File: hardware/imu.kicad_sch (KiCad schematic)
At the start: 4 parts, among them U9 LSM6DSV16XTR

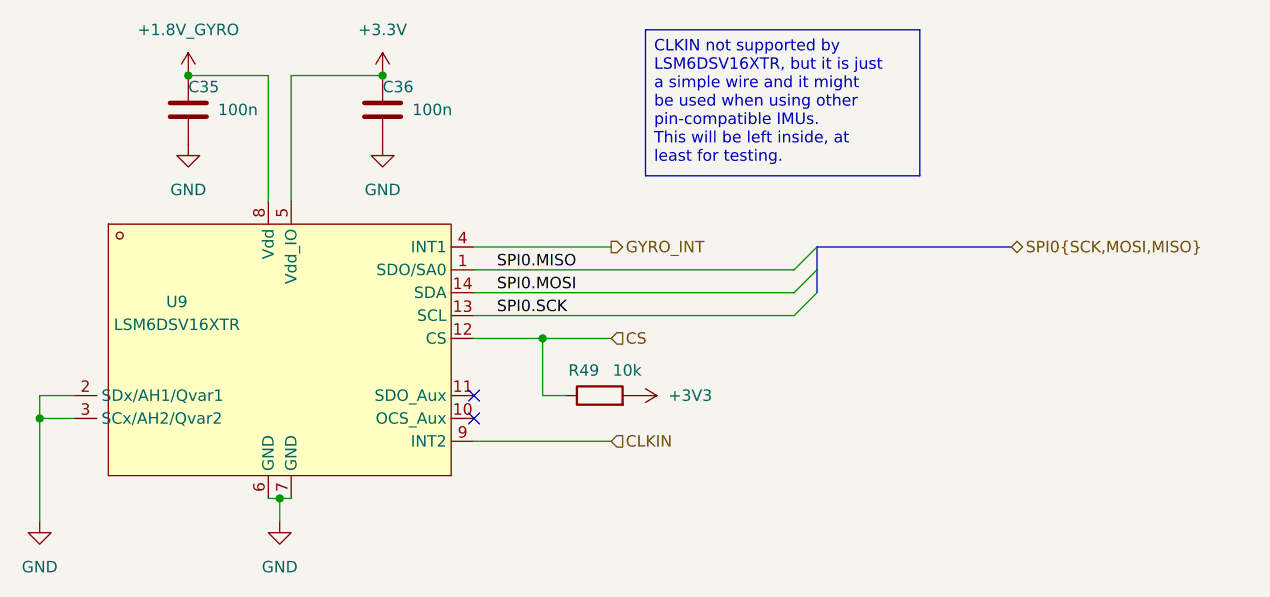
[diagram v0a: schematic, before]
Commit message: move changes from mini over to "maxi"
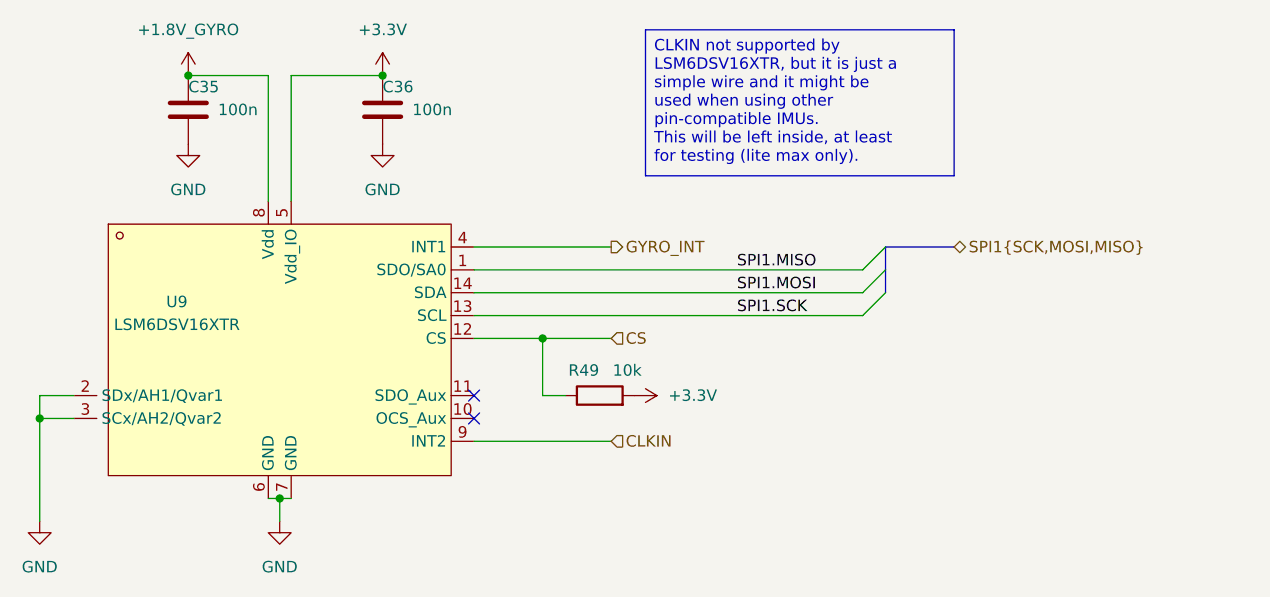
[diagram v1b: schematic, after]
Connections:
- net +3V3 is gone; now on net +3.3V: R49.2
- net SPI0.MISO renamed SPI1.MISO
- net SPI0.MOSI renamed SPI1.MOSI
- net SPI0.SCK renamed SPI1.SCK
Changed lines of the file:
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@@
 	(generator_version "10.0")
 	(paper "A5")
-	(text_box "CLKIN not supported by LSM6DSV16XTR, but it is just a simple wire and it might be used when using other pin-compatible IMUs.\nThis will be left inside, at least for testing."
+	(text_box "CLKIN not supported by LSM6DSV16XTR, but it is just a simple wire and it might be used when using other pin-compatible IMUs.\nThis will be left inside, at least for testing (lite max only)."
 		(exclude_from_sim no)
 		(at 113.03 38.1 0)
-		(size 30.48 16.2161)
+		(size 34.29 16.2161)
 		(margins 0.9525 0.9525 0.9525 0.9525)
 		(stroke
@@
 	)
 	(bus_entry
-		(at 129.54 67.31)
+		(at 137.16 64.77)
 		(size 2.54 -2.54)
 		(stroke
@@
 	)
 	(bus_entry
-		(at 129.54 64.77)
+		(at 137.16 69.85)
 		(size 2.54 -2.54)
 		(stroke
@@
 	)
 	(bus_entry
-		(at 129.54 69.85)
+		(at 137.16 67.31)
 		(size 2.54 -2.54)
 		(stroke
@@
 		)
 	)
-	(wire
-		(pts
-			(xy 93.98 64.77) (xy 129.54 64.77)
+	(bus
+		(pts
+			(xy 139.7 64.77) (xy 139.7 67.31)
 		)
 		(stroke
@@
 		)
 	)
-	(wire
-		(pts
-			(xy 93.98 69.85) (xy 129.54 69.85)
+	(bus
+		(pts
+			(xy 139.7 62.23) (xy 139.7 64.77)
+		)
+		(stroke
+			(width 0)
+			(type default)
+		)
+	)
+	(bus
+		(pts
+			(xy 147.32 62.23) (xy 139.7 62.23)
 		)
 		(stroke
@@
 	(wire
 		(pts
+			(xy 93.98 64.77) (xy 137.16 64.77)
+		)
+		(stroke
+			(width 0)
+			(type default)
+		)
+	)
+	(wire
+		(pts
+			(xy 93.98 67.31) (xy 137.16 67.31)
+		)
+		(stroke
+			(width 0)
+			(type default)
+		)
+	)
+	(wire
+		(pts
 			(xy 93.98 62.23) (xy 109.22 62.23)
 		)
@@
 		)
 	)
-	(bus
-		(pts
-			(xy 132.08 64.77) (xy 132.08 62.23)
-		)
-		(stroke
-			(width 0)
-			(type default)
-		)
-	)
 	(wire
 		(pts
@@
 		)
 	)
-	(bus
-		(pts
-			(xy 132.08 62.23) (xy 153.67 62.23)
-		)
-		(stroke
-			(width 0)
-			(type default)
-		)
-	)
 	(wire
 		(pts
@@
 		)
 	)
-	(bus
-		(pts
-			(xy 132.08 67.31) (xy 132.08 64.77)
-		)
-		(stroke
-			(width 0)
-			(type default)
-		)
-	)
 	(wire
 		(pts
@@
 	(wire
 		(pts
-			(xy 93.98 67.31) (xy 129.54 67.31)
-		)
-		(stroke
-			(width 0)
-			(type default)
-		)
-	)
-	(wire
-		(pts
 			(xy 45.72 78.74) (xy 49.53 78.74)
 		)
@@
 	(wire
 		(pts
+			(xy 93.98 69.85) (xy 137.16 69.85)
+		)
+		(stroke
+			(width 0)
+			(type default)
+		)
+	)
+	(wire
+		(pts
 			(xy 71.12 43.18) (xy 71.12 57.15)
 		)
@@
 		)
 	)
-	(label "SPI0.MOSI"
-		(at 96.52 67.31 0)
+	(label "SPI1.MISO"
+		(at 123.19 64.77 0)
 		(effects
 			(font
@@
 		)
 	)
-	(label "SPI0.MISO"
-		(at 96.52 64.77 0)
+	(label "SPI1.MOSI"
+		(at 123.19 67.31 0)
 		(effects
 			(font
@@
 		)
 	)
-	(label "SPI0.SCK"
-		(at 96.52 69.85 0)
+	(label "SPI1.SCK"
+		(at 123.19 69.85 0)
 		(effects
 			(font
@@
 			)
 			(justify left bottom)
+		)
+	)
+	(hierarchical_label "SPI1{SCK,MOSI,MISO}"
+		(shape bidirectional)
+		(at 147.32 62.23 0)
+		(effects
+			(font
+				(size 1.27 1.27)
+			)
+			(justify left)
 		)
 	)
@@
 		(shape input)
 		(at 109.22 83.82 0)
-		(effects
-			(font
-				(size 1.27 1.27)
-			)
-			(justify left)
-		)
-	)
-	(hierarchical_label "SPI0{SCK,MOSI,MISO}"
-		(shape bidirectional)
-		(at 153.67 62.23 0)
 		(effects
 			(font
@@
 	)
 	(symbol
+		(lib_id "power:+3.3V")
+		(at 111.76 78.74 270)
+		(unit 1)
+		(body_style 1)
+		(exclude_from_sim no)
+		(in_bom yes)
+		(on_board yes)
+		(in_pos_files yes)
+		(dnp no)
+		(fields_autoplaced yes)
+		(property "Reference" "#PWR0156"
+			(at 107.95 78.74 0)
+			(hide yes)
+			(show_name no)
+			(do_not_autoplace no)
+			(effects
+				(font
+					(size 1.27 1.27)
+				)
+			)
+		)
+		(property "Value" "+3.3V"
+			(at 115.57 78.7399 90)
+			(show_name no)
+			(do_not_autoplace no)
+			(effects
+				(font
+					(size 1.27 1.27)
+				)
+				(justify left)
+			)
+		)
+		(property "Footprint" ""
+			(at 111.76 78.74 0)
+			(hide yes)
+			(show_name no)
+			(do_not_autoplace no)
+			(effects
+				(font
+					(size 1.27 1.27)
+				)
+			)
+		)
+		(property "Datasheet" ""
+			(at 111.76 78.74 0)
+			(hide yes)
+			(show_name no)
+			(do_not_autoplace no)
+			(effects
+				(font
+					(size 1.27 1.27)
+				)
+			)
+		)
+		(property "Description" "Power symbol creates a global label with name \"+3.3V\""
+			(at 111.76 78.74 0)
+			(hide yes)
+			(show_name no)
+			(do_not_autoplace no)
+			(effects
+				(font
+					(size 1.27 1.27)
+				)
+			)
+		)
+		(pin "1"
+		)
+		(instances
+			(project "OpenFC"
+				(path "/fb88b6f9-ee39-4640-a9d4-04a17ceeac64/757ed1e6-9a5f-4a0e-a946-254eae8dfb0d"
+					(reference "#PWR0156")
+					(unit 1)
+				)
+			)
+		)
+	)
+	(symbol
 		(lib_id "power:GND")
 		(at 45.72 92.71 0)
@@
 					(unit 1)
 				)
-			)
-		)
-	)
-	(symbol
-		(lib_id "power:+3V3")
-		(at 111.76 78.74 270)
-		(unit 1)
-		(body_style 1)
-		(exclude_from_sim no)
-		(in_bom yes)
-		(on_board yes)
-		(in_pos_files yes)
-		(dnp no)
-		(fields_autoplaced yes)
-		(property "Reference" "#PWR07"
-			(at 107.95 78.74 0)
-			(hide yes)
-			(show_name no)
-			(do_not_autoplace no)
-			(effects
-				(font
-					(size 1.27 1.27)
-				)
-			)
-		)
-		(property "Value" "+3V3"
-			(at 115.57 78.7399 90)
-			(show_name no)
-			(do_not_autoplace no)
-			(effects
-				(font
-					(size 1.27 1.27)
-				)
-				(justify left)
-			)
-		)
-		(property "Footprint" ""
-			(at 111.76 78.74 0)
-			(hide yes)
-			(show_name no)
-			(do_not_autoplace no)
-			(effects
-				(font
-					(size 1.27 1.27)
-				)
-			)
-		)
-		(property "Datasheet" ""
-			(at 111.76 78.74 0)
-			(hide yes)
-			(show_name no)
-			(do_not_autoplace no)
-			(effects
-				(font
-					(size 1.27 1.27)
-				)
-			)
-		)
-		(property "Description" "Power symbol creates a global label with name \"+3V3\""
-			(at 111.76 78.74 0)
-			(hide yes)
-			(show_name no)
-			(do_not_autoplace no)
-			(effects
-				(font
-					(size 1.27 1.27)
-				)
-			)
-		)
-		(pin "1"
-		)
-		(instances
-			(project "OpenFC"
-				(path "/fb88b6f9-ee39-4640-a9d4-04a17ceeac64/757ed1e6-9a5f-4a0e-a946-254eae8dfb0d"
-					(reference "#PWR07")
-					(unit 1)
-				)

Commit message: routing
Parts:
- renumbered C35 to C33, C36 to C34, R49 to R29
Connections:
- net SPI1.MISO renamed SPI0.MISO
- net SPI1.MOSI renamed SPI0.MOSI
- net SPI1.SCK renamed SPI0.SCK
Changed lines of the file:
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@@
 		)
 	)
-	(label "SPI1.MISO"
+	(label "SPI0.MISO"
 		(at 123.19 64.77 0)
 		(effects
@@
 		)
 	)
-	(label "SPI1.MOSI"
+	(label "SPI0.MOSI"
 		(at 123.19 67.31 0)
 		(effects
@@
 		)
 	)
-	(label "SPI1.SCK"
+	(label "SPI0.SCK"
 		(at 123.19 69.85 0)
 		(effects
@@
 		)
 	)
-	(hierarchical_label "SPI1{SCK,MOSI,MISO}"
+	(hierarchical_label "SPI0{SCK,MOSI,MISO}"
 		(shape bidirectional)
 		(at 147.32 62.23 0)
@@
 		(in_pos_files yes)
 		(dnp no)
-		(property "Reference" "R49"
+		(property "Reference" "R29"
 			(at 106.172 75.946 90)
 			(show_name no)
@@
 			(project "OpenFC"
 				(path "/fb88b6f9-ee39-4640-a9d4-04a17ceeac64/757ed1e6-9a5f-4a0e-a946-254eae8dfb0d"
-					(reference "R49")
+					(reference "R29")
 					(unit 1)
 				)
@@
 		(dnp no)
 		(fields_autoplaced yes)
-		(property "Reference" "#PWR0130"
+		(property "Reference" "#PWR0121"
 			(at 83.82 46.99 0)
 			(hide yes)
@@
 			(project "OpenFC"
 				(path "/fb88b6f9-ee39-4640-a9d4-04a17ceeac64/757ed1e6-9a5f-4a0e-a946-254eae8dfb0d"
-					(reference "#PWR0130")
+					(reference "#PWR0121")
 					(unit 1)
 				)
@@
 		(dnp no)
 		(fields_autoplaced yes)
-		(property "Reference" "#PWR0156"
+		(property "Reference" "#PWR0123"
 			(at 107.95 78.74 0)
 			(hide yes)
@@
 			(project "OpenFC"
 				(path "/fb88b6f9-ee39-4640-a9d4-04a17ceeac64/757ed1e6-9a5f-4a0e-a946-254eae8dfb0d"
-					(reference "#PWR0156")
+					(reference "#PWR0123")
 					(unit 1)
 				)
@@
 		(dnp no)
 		(fields_autoplaced yes)
-		(property "Reference" "#PWR0125"
+		(property "Reference" "#PWR0117"
 			(at 45.72 99.06 0)
 			(hide yes)
@@
 			(project "OpenFC"
 				(path "/fb88b6f9-ee39-4640-a9d4-04a17ceeac64/757ed1e6-9a5f-4a0e-a946-254eae8dfb0d"
-					(reference "#PWR0125")
+					(reference "#PWR0117")
 					(unit 1)
 				)
@@
 		(dnp no)
 		(fields_autoplaced yes)
-		(property "Reference" "#PWR0131"
+		(property "Reference" "#PWR0122"
 			(at 83.82 57.15 0)
 			(hide yes)
@@
 			(project "OpenFC"
 				(path "/fb88b6f9-ee39-4640-a9d4-04a17ceeac64/757ed1e6-9a5f-4a0e-a946-254eae8dfb0d"
-					(reference "#PWR0131")
+					(reference "#PWR0122")
 					(unit 1)
 				)
@@
 		(in_pos_files yes)
 		(dnp no)
-		(property "Reference" "C35"
+		(property "Reference" "C33"
 			(at 62.23 44.45 0)
 			(show_name no)
@@
 			(project "OpenFC"
 				(path "/fb88b6f9-ee39-4640-a9d4-04a17ceeac64/757ed1e6-9a5f-4a0e-a946-254eae8dfb0d"
-					(reference "C35")
+					(reference "C33")
 					(unit 1)
 				)
@@
 		(dnp no)
 		(fields_autoplaced yes)
-		(property "Reference" "#PWR0127"
+		(property "Reference" "#PWR0118"
 			(at 62.23 46.99 0)
 			(hide yes)
@@
 			(project "OpenFC"
 				(path "/fb88b6f9-ee39-4640-a9d4-04a17ceeac64/757ed1e6-9a5f-4a0e-a946-254eae8dfb0d"
-					(reference "#PWR0127")
+					(reference "#PWR0118")
 					(unit 1)
 				)
@@
 		(dnp no)
 		(fields_autoplaced yes)
-		(property "Reference" "#PWR0126"
+		(property "Reference" "#PWR0119"
 			(at 62.23 57.15 0)
 			(hide yes)
@@
 			(project "OpenFC"
 				(path "/fb88b6f9-ee39-4640-a9d4-04a17ceeac64/757ed1e6-9a5f-4a0e-a946-254eae8dfb0d"
-					(reference "#PWR0126")
+					(reference "#PWR0119")
 					(unit 1)
 				)
@@
 		(dnp no)
 		(fields_autoplaced yes)
-		(property "Reference" "#PWR0128"
+		(property "Reference" "#PWR0120"
 			(at 72.39 99.06 0)
 			(hide yes)
@@
 			(project "OpenFC"
 				(path "/fb88b6f9-ee39-4640-a9d4-04a17ceeac64/757ed1e6-9a5f-4a0e-a946-254eae8dfb0d"
-					(reference "#PWR0128")
+					(reference "#PWR0120")
 					(unit 1)
 				)
@@
 		(in_pos_files yes)
 		(dnp no)
-		(property "Reference" "C36"
+		(property "Reference" "C34"
 			(at 83.82 44.45 0)
 			(show_name no)
@@
 			(project "OpenFC"
 				(path "/fb88b6f9-ee39-4640-a9d4-04a17ceeac64/757ed1e6-9a5f-4a0e-a946-254eae8dfb0d"
-					(reference "C36")
+					(reference "C34")
 					(unit 1)
 				)
